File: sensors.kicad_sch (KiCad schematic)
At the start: 16 parts, among them U4 LSM6DSV16XTR, U5 LIS2MDLTR

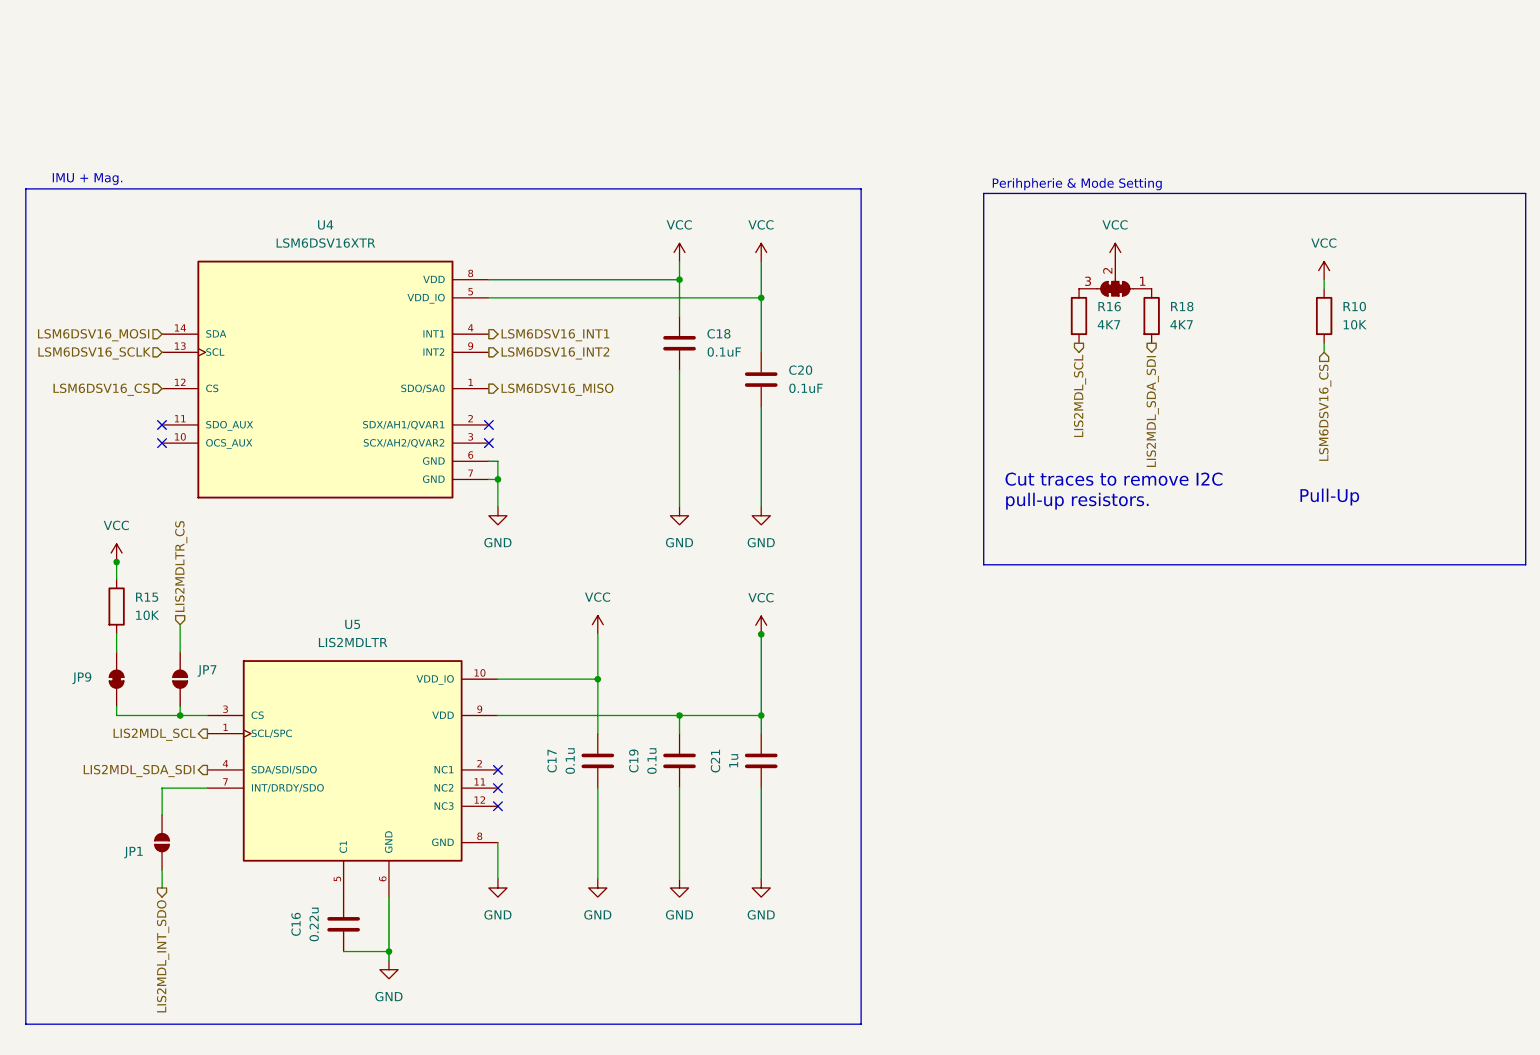
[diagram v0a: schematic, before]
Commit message: Optimize power path component arrangement
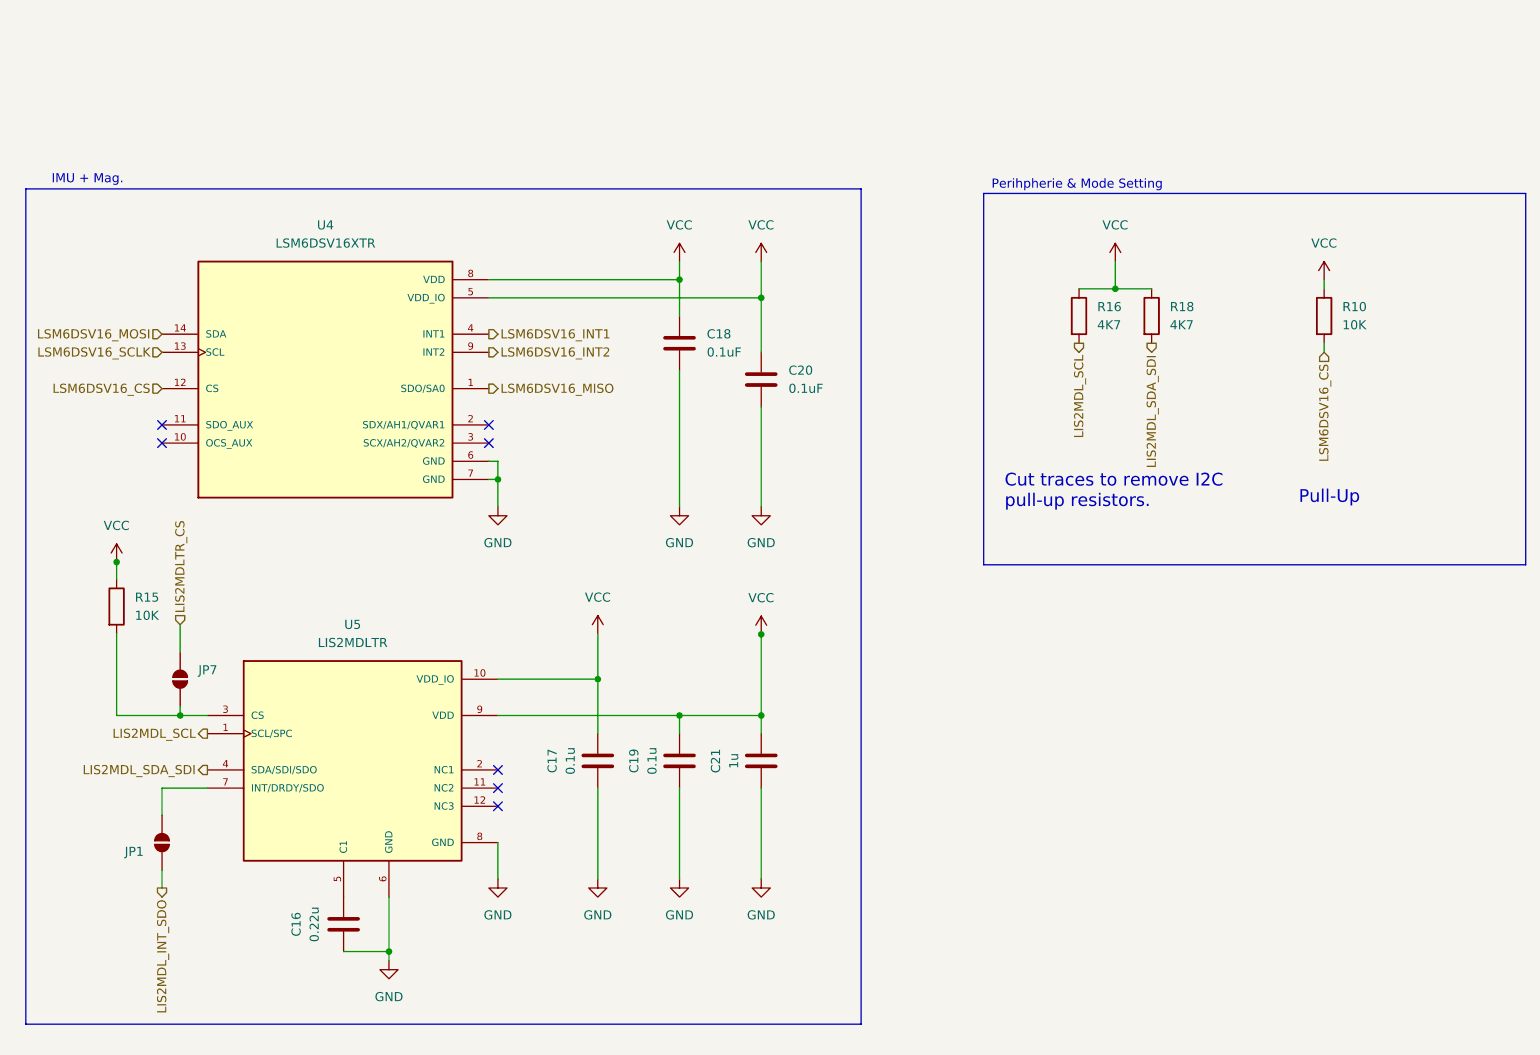
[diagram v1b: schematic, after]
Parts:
- removed JP6: SolderJumper_3_Bridged123, Jumper:SolderJumper-3_P1.3mm_Bridged123_RoundedPad1.0x1.5mm, symbol Jumper:SolderJumper_3_Bridged123
- removed JP9: SolderJumper_2_Bridged, Jumper:SolderJumper-2_P1.3mm_Bridged_RoundedPad1.0x1.5mm, symbol Jumper:SolderJumper_2_Bridged
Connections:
- net VCC: now also R16.1, R18.1
- net at R15.2: now also JP7.2 (B), U5.3 (CS)
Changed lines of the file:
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@@
+	)
+	(junction
+		(at 168.91 64.77)
+		(diameter 0)
+		(color 0 0 0 0)
 	)
 	(junction
@@
 	(wire
 		(pts
-			(xy 29.21 113.03) (xy 29.21 115.57)
+			(xy 29.21 113.03) (xy 29.21 124.46)
 		)
 		(stroke
@@
 	(wire
 		(pts
+			(xy 168.91 64.77) (xy 173.99 64.77)
+		)
+		(stroke
+			(width 0)
+			(type default)
+		)
+	)
+	(wire
+		(pts
 			(xy 119.38 113.106) (xy 119.38 124.46)
 		)
@@
 	(wire
 		(pts
-			(xy 29.21 123.19) (xy 29.21 124.46)
+			(xy 168.91 64.77) (xy 168.91 60.96)
 		)
 		(stroke
@@
 		(pts
 			(xy 81.28 66.04) (xy 119.38 66.04)
+		)
+		(stroke
+			(width 0)
+			(type default)
+		)
+	)
+	(wire
+		(pts
+			(xy 163.83 64.77) (xy 168.91 64.77)
 		)
 		(stroke
@@
 	)
 	(symbol
-		(lib_id "Jumper:SolderJumper_2_Bridged")
-		(at 29.21 119.38 270)
-		(unit 1)
-		(exclude_from_sim no)
-		(in_bom no)
-		(on_board yes)
-		(dnp no)
-		(property "Reference" "JP9"
-			(at 23.114 119.126 90)
-			(effects
-				(font
-					(size 1.27 1.27)
-				)
-				(justify left)
-			)
-		)
-		(property "Value" "SolderJumper_2_Bridged"
-			(at 1.524 119.634 90)
-			(effects
-				(font
-					(size 1.27 1.27)
-				)
-				(justify left)
-				(hide yes)
-			)
-		)
-		(property "Footprint" "Jumper:SolderJumper-2_P1.3mm_Bridged_RoundedPad1.0x1.5mm"
-			(at 29.21 119.38 0)
-			(effects
-				(font
-					(size 1.27 1.27)
-				)
-				(hide yes)
-			)
-		)
-		(property "Datasheet" "~"
-			(at 29.21 119.38 0)
-			(effects
-				(font
-					(size 1.27 1.27)
-				)
-				(hide yes)
-			)
-		)
-		(property "Description" "Solder Jumper, 2-pole, closed/bridged"
-			(at 29.21 119.38 0)
-			(effects
-				(font
-					(size 1.27 1.27)
-				)
-				(hide yes)
-			)
-		)
-		(pin "1"
-		)
-		(pin "2"
-		)
-		(instances
-			(project "imuTag"
-				(path "/b0790ebf-2d8c-4cec-b4ed-465f5b1bb1fd/95deafee-4d41-41f8-aa41-aae5f7671aba"
-					(reference "JP9")
-					(unit 1)
-				)
-			)
-		)
-	)
-	(symbol
 		(lib_id "power:VCC")
 		(at 96.52 113.03 0)
@@
 					(unit 1)
 				)
-			)
-		)
-	)
-	(symbol
-		(lib_id "Jumper:SolderJumper_3_Bridged123")
-		(at 168.91 64.77 180)
-		(unit 1)
-		(exclude_from_sim no)
-		(in_bom no)
-		(on_board yes)
-		(dnp no)
-		(property "Reference" "JP6"
-			(at 169.164 47.498 0)
-			(effects
-				(font
-					(size 1.27 1.27)
-				)
-				(hide yes)
-			)
-		)
-		(property "Value" "SolderJumper_3_Bridged123"
-			(at 169.164 50.038 0)
-			(effects
-				(font
-					(size 1.27 1.27)
-				)
-				(hide yes)
-			)
-		)
-		(property "Footprint" "Jumper:SolderJumper-3_P1.3mm_Bridged123_RoundedPad1.0x1.5mm"
-			(at 168.91 64.77 0)
-			(effects
-				(font
-					(size 1.27 1.27)
-				)
-				(hide yes)
-			)
-		)
-		(property "Datasheet" "~"
-			(at 168.91 64.77 0)
-			(effects
-				(font
-					(size 1.27 1.27)
-				)
-				(hide yes)
-			)
-		)
-		(property "Description" "Solder Jumper, 3-pole, pins 1+2+3 closed/bridged"
-			(at 168.91 64.77 0)
-			(effects
-				(font
-					(size 1.27 1.27)
-				)
-				(hide yes)
-			)
-		)
-		(pin "2"
-		)
-		(pin "1"
-		)
-		(pin "3"
-		)
-		(instances
-			(project "imuTag"
-				(path "/b0790ebf-2d8c-4cec-b4ed-465f5b1bb1fd/95deafee-4d41-41f8-aa41-aae5f7671aba"
-					(reference "JP6")
-					(unit 1)
-				)

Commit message: draw Important Tracks
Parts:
- C17, C19, C20: footprint Capacitor_SMD:C_0603_1608Metric -> Capacitor_SMD:C_0402_1005Metric
- R10, R15, R16, R18: footprint Resistor_SMD:R_0603_1608Metric -> Resistor_SMD:R_0402_1005Metric
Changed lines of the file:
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@@
 			)
 		)
-		(property "Footprint" "Resistor_SMD:R_0603_1608Metric"
+		(property "Footprint" "Resistor_SMD:R_0402_1005Metric"
 			(at 196.342 68.58 90)
 			(effects
@@
 			)
 		)
-		(property "Footprint" "Resistor_SMD:R_0603_1608Metric"
+		(property "Footprint" "Resistor_SMD:R_0402_1005Metric"
 			(at 162.052 68.58 90)
 			(effects
@@
 			)
 		)
-		(property "Footprint" "Capacitor_SMD:C_0603_1608Metric"
+		(property "Footprint" "Capacitor_SMD:C_0402_1005Metric"
 			(at 106.9848 127 0)
 			(effects
@@
 			)
 		)
-		(property "Footprint" "Resistor_SMD:R_0603_1608Metric"
+		(property "Footprint" "Resistor_SMD:R_0402_1005Metric"
 			(at 27.432 109.22 90)
 			(effects
@@
 			)
 		)
-		(property "Footprint" "Capacitor_SMD:C_0603_1608Metric"
+		(property "Footprint" "Capacitor_SMD:C_0402_1005Metric"
 			(at 120.3452 81.28 0)
 			(effects
@@
 			)
 		)
-		(property "Footprint" "Capacitor_SMD:C_0603_1608Metric"
+		(property "Footprint" "Capacitor_SMD:C_0402_1005Metric"
 			(at 95.5548 127 0)
 			(effects
@@
 			)
 		)
-		(property "Footprint" "Resistor_SMD:R_0603_1608Metric"
+		(property "Footprint" "Resistor_SMD:R_0402_1005Metric"
 			(at 172.212 68.58 90)
 			(effects

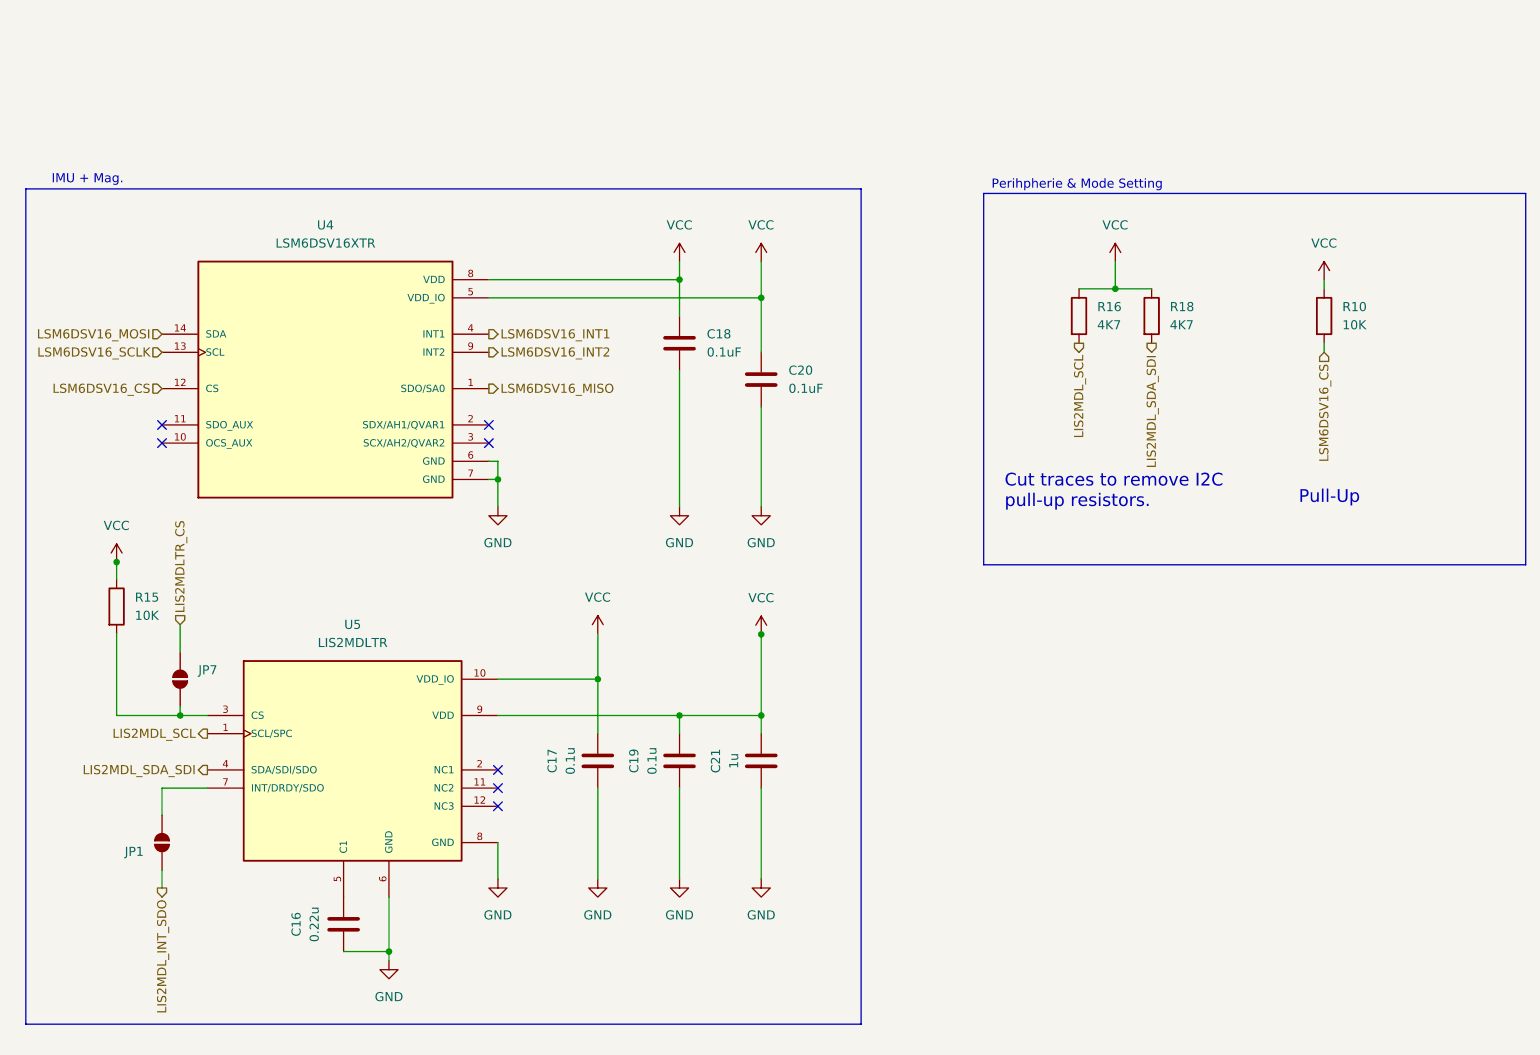
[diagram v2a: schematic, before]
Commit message: feat: imuTag mini PCBA v1.0 – initial release
PCB layout, schematics (imuTag + sensors), custom EasyEDA symbol/footprint libraries with 3D models, design rules, and production outputs (BOM, placement, netlist).
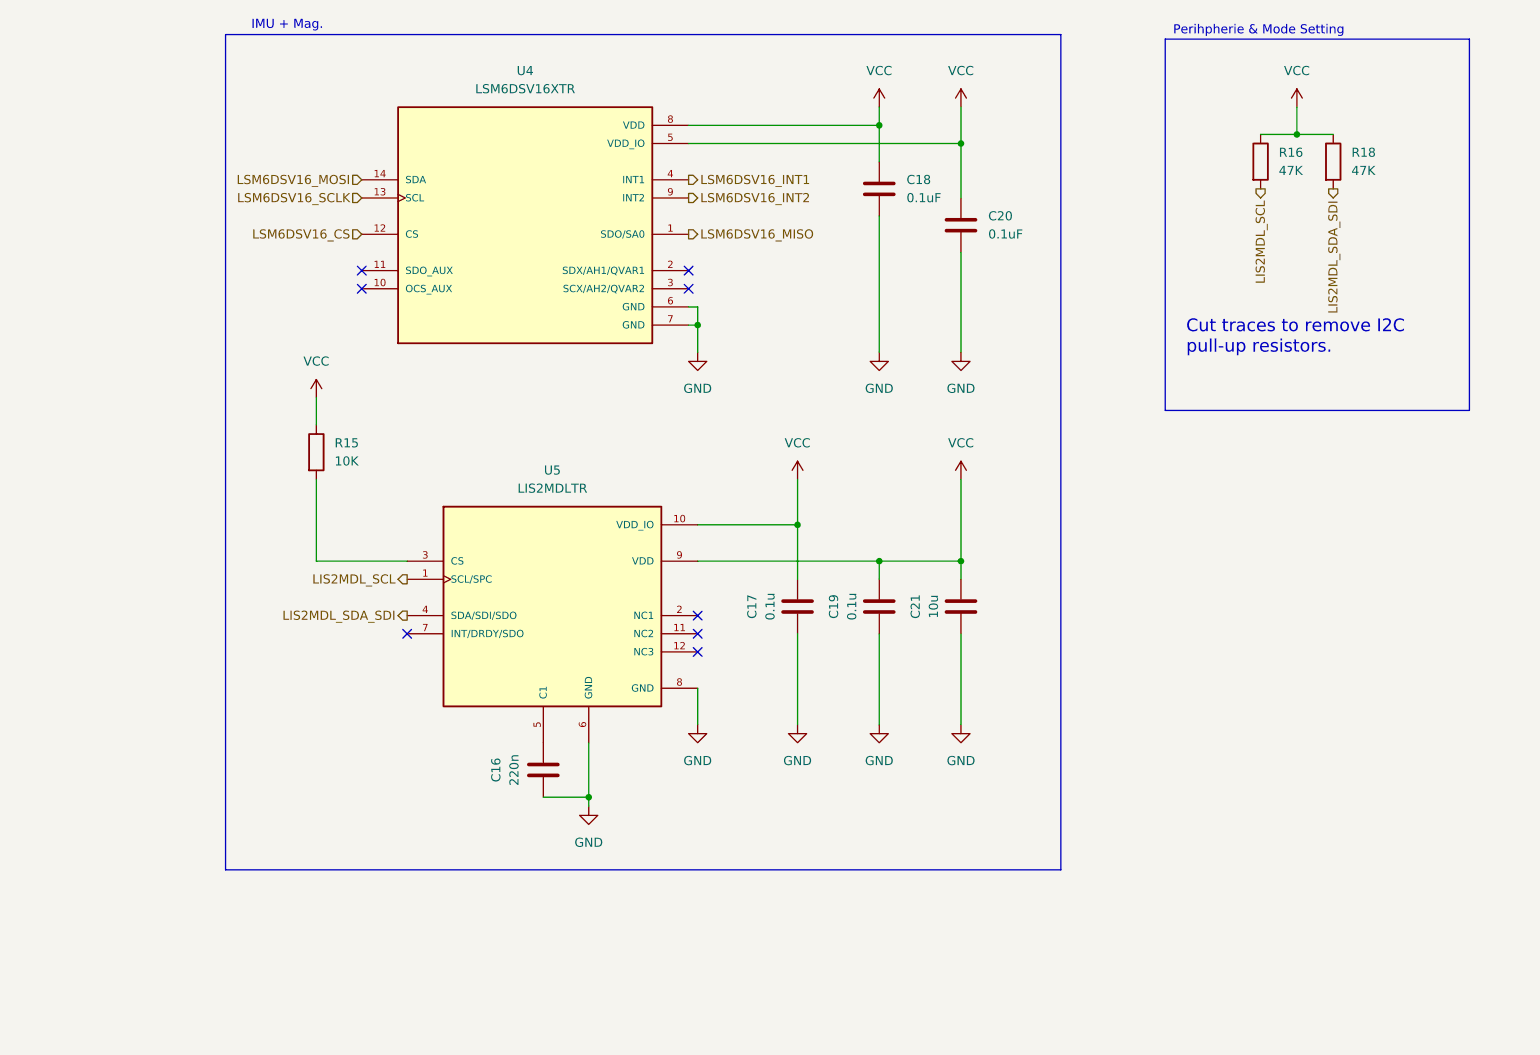
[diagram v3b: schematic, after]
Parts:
- removed JP1, JP7: SolderJumper_2_Open, Jumper:SolderJumper-2_P1.3mm_Open_Pad1.0x1.5mm, symbol Jumper:SolderJumper_2_Open
- removed R10: 10K, Resistor_SMD:R_0402_1005Metric, symbol Device:R
- C16: value 0.22u -> 220n; footprint Capacitor_SMD:C_0603_1608Metric -> Capacitor_SMD:C_0402_1005Metric
- C18: footprint Capacitor_SMD:C_0603_1608Metric -> Capacitor_SMD:C_0402_1005Metric
- C21: value 1u -> 10u
- R16, R18: value 4K7 -> 47K
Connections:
- no-connect marks 7 -> 8
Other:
- note removed: "Pull-Up"
- moved on the sheet: C16, C17, C18, C19, C20, C21, R15, R16, R18, U4, U5
